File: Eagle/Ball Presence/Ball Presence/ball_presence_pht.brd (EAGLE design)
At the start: 26.4 x 24.2 mm, 7 parts, among them Q1 VEMT2520X01, Q2 VEMT2520X01

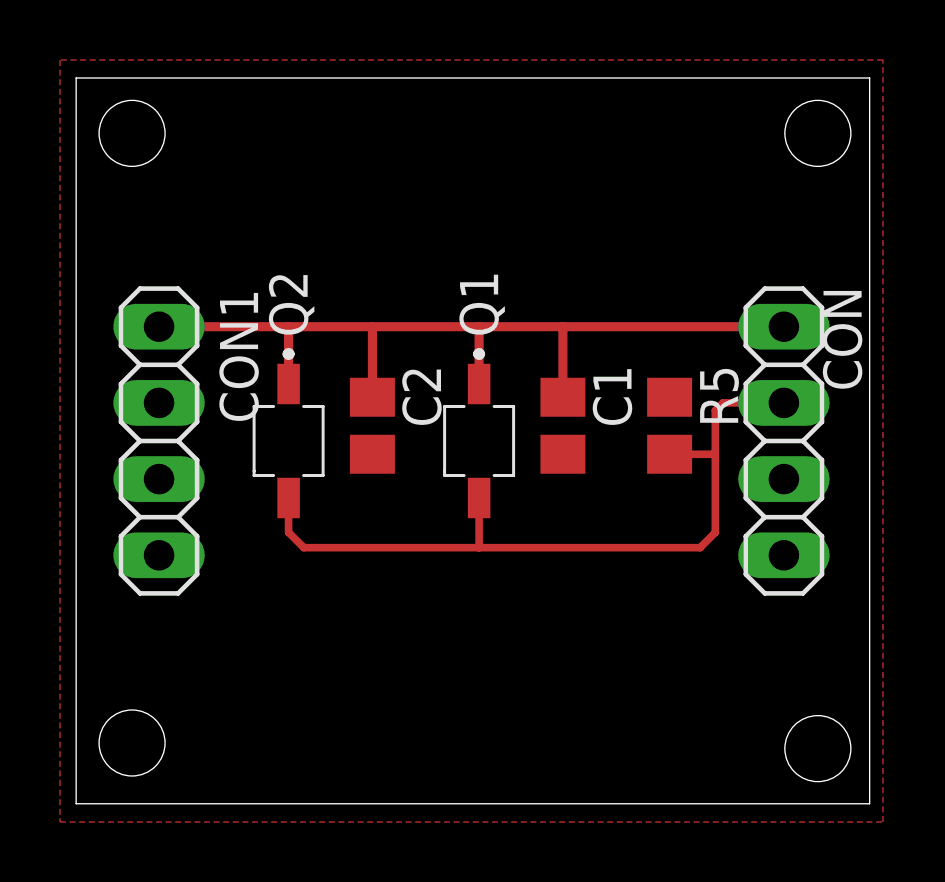
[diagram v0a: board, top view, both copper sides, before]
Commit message: ball presence sensor v1.0
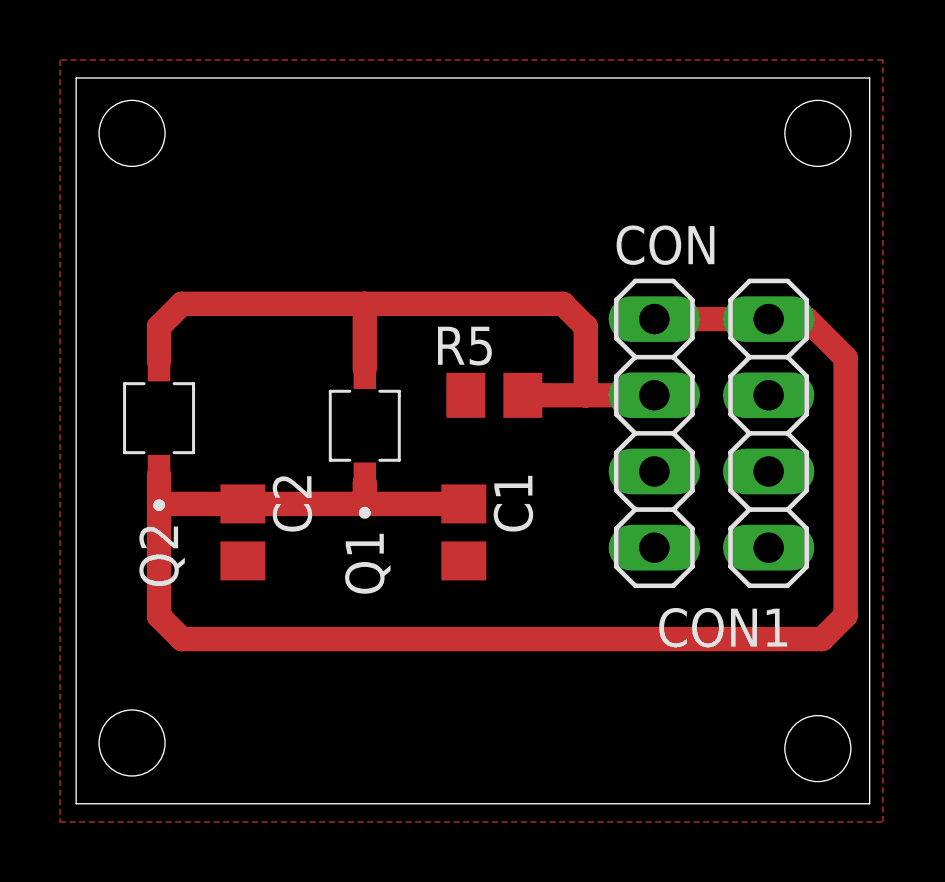
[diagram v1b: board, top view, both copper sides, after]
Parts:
- moved CON1 20.3 mm to (55.1, 13.0)
- moved R5 5.93 mm to (46.0, 14.2), turned to 0 degrees
- moved C2 5.59 mm to (37.6, 9.65)
- moved C1 4.85 mm to (45.0, 9.65)
- moved Q2 4.38 mm to (34.8, 13.5), turned to 90 degrees
- moved CON 4.33 mm to (51.3, 13.0)
- moved Q1 3.84 mm to (41.7, 13.2), turned to 90 degrees
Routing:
- net V+: track 29.4 -> 54.8 mm
- net SIG1: track 25.5 -> 24.8 mm
